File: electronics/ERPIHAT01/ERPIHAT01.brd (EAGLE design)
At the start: 65 x 56 mm, 34 parts, among them J1 CONN-RECT-4PINJST-PH-2MM, J2 CONN-RECT-4PINJST-PH-2MM, J3 CONN-HDMI, J4 CON-FFC-SFW15R, J5 CONN-RECT-3PINJST_PH_2MM, K1 RPI_GPIO, Q1 DMG2305UX, Q2 DMMT5401, Q3 MMBT2222A, U1 EEPROM24, U6 LM2576-D2T

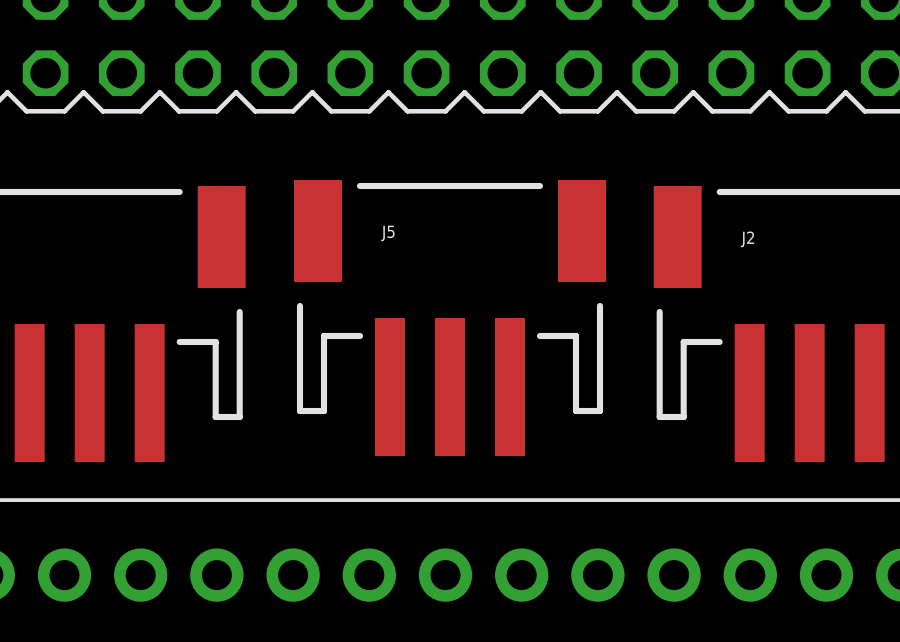
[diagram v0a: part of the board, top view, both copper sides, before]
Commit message: Changed power connector from 3-pin to 2-pin
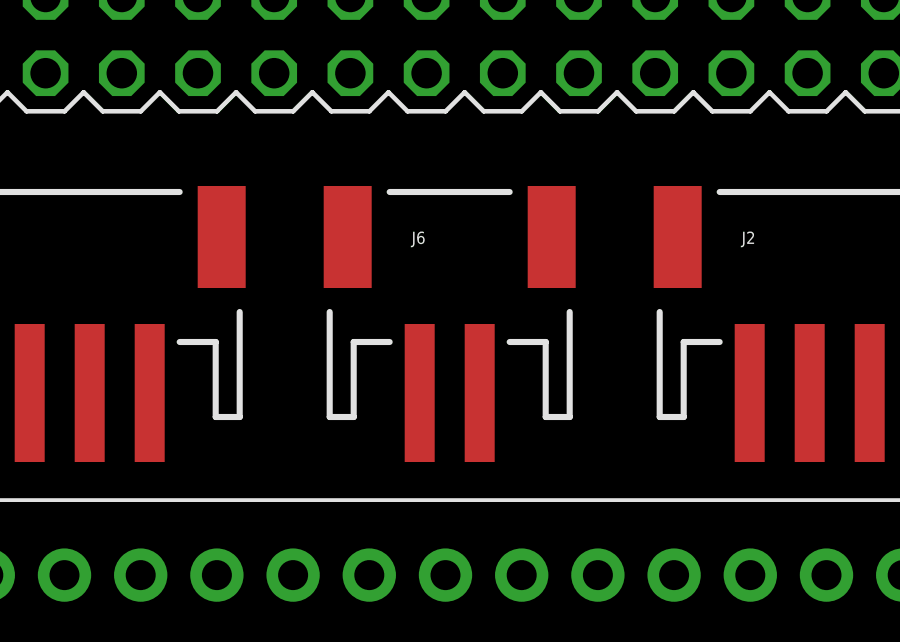
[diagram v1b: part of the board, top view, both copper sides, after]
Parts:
- removed J5: CONN-RECT-3PINJST_PH_2MM, FirePick:CONN-JST_PH-2.0MM-3PIN-SMT-RA
- added J6: CONN-RECT-2PIN, FirePick:CONN-JST_PH-2.0MM-2PIN-SMT-RA
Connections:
- net 12V: now also J6.2; no longer J5.1
- net GND: now also J6.1; no longer J5.3
- net GPIO7: no longer J5.2
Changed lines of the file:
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@@
 <element name="D1" library="diode" package="DO-214AC" value="" x="54" y="29" rot="R180"/>
 <element name="C4" library="rcl" package="PANASONIC_D" value="470uF" x="38" y="27" rot="R90"/>
-<element name="J5" library="FirePick" package="CONN-JST_PH-2.0MM-3PIN-SMT-RA" value="CONN-RECT-3PINJST_PH_2MM" x="32" y="43"/>
+<element name="J6" library="FirePick" package="CONN-JST_PH-2.0MM-2PIN-SMT-RA" value="CONN-RECT-2PIN" x="32" y="43"/>
 </elements>
 <signals>
@@
 <contactref element="D1" pad="A"/>
 <contactref element="C4" pad="-"/>
-<contactref element="J5" pad="3"/>
-<wire x1="78.5025" y1="47.075" x2="80" y2="42.485" width="0" layer="19" extent="1-1"/>
+<contactref element="J6" pad="1"/>
+<wire x1="78.5025" y1="47.075" x2="87" y2="54" width="0" layer="19" extent="1-1"/>
 <wire x1="75.645" y1="46.865" x2="78.5025" y2="47.075" width="0" layer="19" extent="1-1"/>
 <wire x1="74.375" y1="46.865" x2="75.645" y2="46.865" width="0" layer="19" extent="1-1"/>
 <wire x1="73.105" y1="46.865" x2="74.375" y2="46.865" width="0" layer="19" extent="1-1"/>
 <wire x1="71.835" y1="46.865" x2="73.105" y2="46.865" width="0" layer="19" extent="1-1"/>
-<wire x1="56.63" y1="51.23" x2="71.835" y2="46.865" width="0" layer="19" extent="1-1"/>
+<wire x1="73.1" y1="51" x2="73.105" y2="46.865" width="0" layer="19" extent="1-1"/>
+<wire x1="74.1" y1="53" x2="73.1" y2="51" width="0" layer="19" extent="1-1"/>
+<wire x1="70" y1="54" x2="74.1" y2="53" width="0" layer="19" extent="1-1"/>
+<wire x1="80" y1="42.485" x2="78.5025" y2="47.075" width="0" layer="19" extent="1-1"/>
+<wire x1="56.63" y1="51.23" x2="70" y2="54" width="0" layer="19" extent="1-1"/>
 <wire x1="49.01" y1="53.77" x2="56.63" y2="51.23" width="0" layer="19" extent="1-1"/>
 <wire x1="43.93" y1="53.77" x2="49.01" y2="53.77" width="0" layer="19" extent="1-1"/>
 <wire x1="38.85" y1="51.23" x2="43.93" y2="53.77" width="0" layer="19" extent="1-1"/>
-<wire x1="87" y1="54" x2="38.85" y2="51.23" width="0" layer="19" extent="1-1"/>
 <wire x1="31.23" y1="53.77" x2="38.85" y2="51.23" width="0" layer="19" extent="1-1"/>
 <wire x1="23.61" y1="53.77" x2="31.23" y2="53.77" width="0" layer="19" extent="1-1"/>
 <wire x1="18.53" y1="51.23" x2="23.61" y2="53.77" width="0" layer="19" extent="1-1"/>
 <wire x1="13.45" y1="53.77" x2="18.53" y2="51.23" width="0" layer="19" extent="1-1"/>
-<wire x1="70" y1="54" x2="23.61" y2="53.77" width="0" layer="19" extent="1-1"/>
-<wire x1="74.1" y1="53" x2="70" y2="54" width="0" layer="19" extent="1-1"/>
-<wire x1="73.1" y1="51" x2="74.1" y2="53" width="0" layer="19" extent="1-1"/>
-<wire x1="22" y1="40.57" x2="70" y2="54" width="0" layer="19" extent="1-1"/>
+<wire x1="22" y1="40.57" x2="18.53" y2="51.23" width="0" layer="19" extent="1-1"/>
 <wire x1="19.16" y1="34.5" x2="22" y2="40.57" width="0" layer="19" extent="1-1"/>
 <wire x1="18.95" y1="25" x2="19.16" y2="34.5" width="0" layer="19" extent="1-1"/>
-<wire x1="14.81" y1="18.25" x2="18.95" y2="25" width="0" layer="19" extent="1-1"/>
+<wire x1="13.86" y1="22.25" x2="18.95" y2="25" width="0" layer="19" extent="1-1"/>
+<wire x1="14.81" y1="18.25" x2="13.86" y2="22.25" width="0" layer="19" extent="1-1"/>
 <wire x1="14.81" y1="16.75" x2="14.81" y2="18.25" width="0" layer="19" extent="1-1"/>
 <wire x1="14.81" y1="16.25" x2="14.81" y2="16.75" width="0" layer="19" extent="1-1"/>
@@
 <wire x1="14.81" y1="10.75" x2="14.81" y2="11.25" width="0" layer="19" extent="1-1"/>
 <wire x1="13.86" y1="7.75" x2="14.81" y2="10.75" width="0" layer="19" extent="1-1"/>
-<wire x1="13.86" y1="22.25" x2="14.81" y2="18.25" width="0" layer="19" extent="1-1"/>
 <wire x1="8.91" y1="22.85" x2="13.86" y2="22.25" width="0" layer="19" extent="1-1"/>
 <wire x1="8.91" y1="7.15" x2="13.86" y2="7.75" width="0" layer="19" extent="1-1"/>
-<wire x1="9" y1="34.5" x2="8.91" y2="22.85" width="0" layer="19" extent="1-1"/>
 <wire x1="11.825" y1="2" x2="8.91" y2="7.15" width="0" layer="19" extent="1-1"/>
-<wire x1="48" y1="40.57" x2="56.63" y2="51.23" width="0" layer="19" extent="1-1"/>
-<wire x1="56.6" y1="34" x2="48" y2="40.57" width="0" layer="19" extent="1-1"/>
-<wire x1="51.975" y1="29" x2="56.6" y2="34" width="0" layer="19" extent="1-1"/>
+<wire x1="9" y1="34.5" x2="19.16" y2="34.5" width="0" layer="19" extent="1-1"/>
+<wire x1="48" y1="40.57" x2="49.01" y2="53.77" width="0" layer="19" extent="1-1"/>
+<wire x1="47.1" y1="34.5" x2="48" y2="40.57" width="0" layer="19" extent="1-1"/>
+<wire x1="51.975" y1="29" x2="47.1" y2="34.5" width="0" layer="19" extent="1-1"/>
 <wire x1="50.596" y1="23.33" x2="51.975" y2="29" width="0" layer="19" extent="1-1"/>
 <wire x1="54" y1="23.33" x2="50.596" y2="23.33" width="0" layer="19" extent="1-1"/>
-<wire x1="47.1" y1="34.5" x2="51.975" y2="29" width="0" layer="19" extent="1-1"/>
+<wire x1="56.6" y1="34" x2="51.975" y2="29" width="0" layer="19" extent="1-1"/>
 <wire x1="54" y1="13" x2="54" y2="23.33" width="0" layer="19" extent="1-1"/>
 <wire x1="40.5" y1="18" x2="50.596" y2="23.33" width="0" layer="19" extent="1-1"/>
@@
 <wire x1="40.5" y1="9" x2="40.5" y2="12" width="0" layer="19" extent="1-1"/>
 <wire x1="38" y1="24.6" x2="40.5" y2="18" width="0" layer="19" extent="1-1"/>
-<wire x1="30.01" y1="40.77" x2="8.91" y2="7.15" width="0" layer="19" extent="1-1"/>
+<wire x1="33" y1="40.57" x2="8.91" y2="7.15" width="0" layer="19" extent="1-1"/>
 </signal>
 <signal name="+3V3">
@@
 <signal name="GPIO7">
 <contactref element="K1" pad="26"/>
-<contactref element="J5" pad="2"/>
-<wire x1="32.01" y1="40.77" x2="38.85" y2="53.77" width="0" layer="19" extent="1-1"/>
 </signal>
 <signal name="GPIO12">
@@
 <contactref element="C7" pad="+"/>
 <contactref element="U6" pad="1"/>
-<contactref element="J5" pad="1"/>
+<contactref element="J6" pad="2"/>
 <wire x1="57.404" y1="23.33" x2="61.4" y2="34" width="0" layer="19" extent="1-1"/>
-<wire x1="34.01" y1="40.77" x2="57.404" y2="23.33" width="0" layer="19" extent="1-1"/>
+<wire x1="31" y1="40.57" x2="57.404" y2="23.33" width="0" layer="19" extent="1-1"/>
 </signal>
 <signal name="N$7">

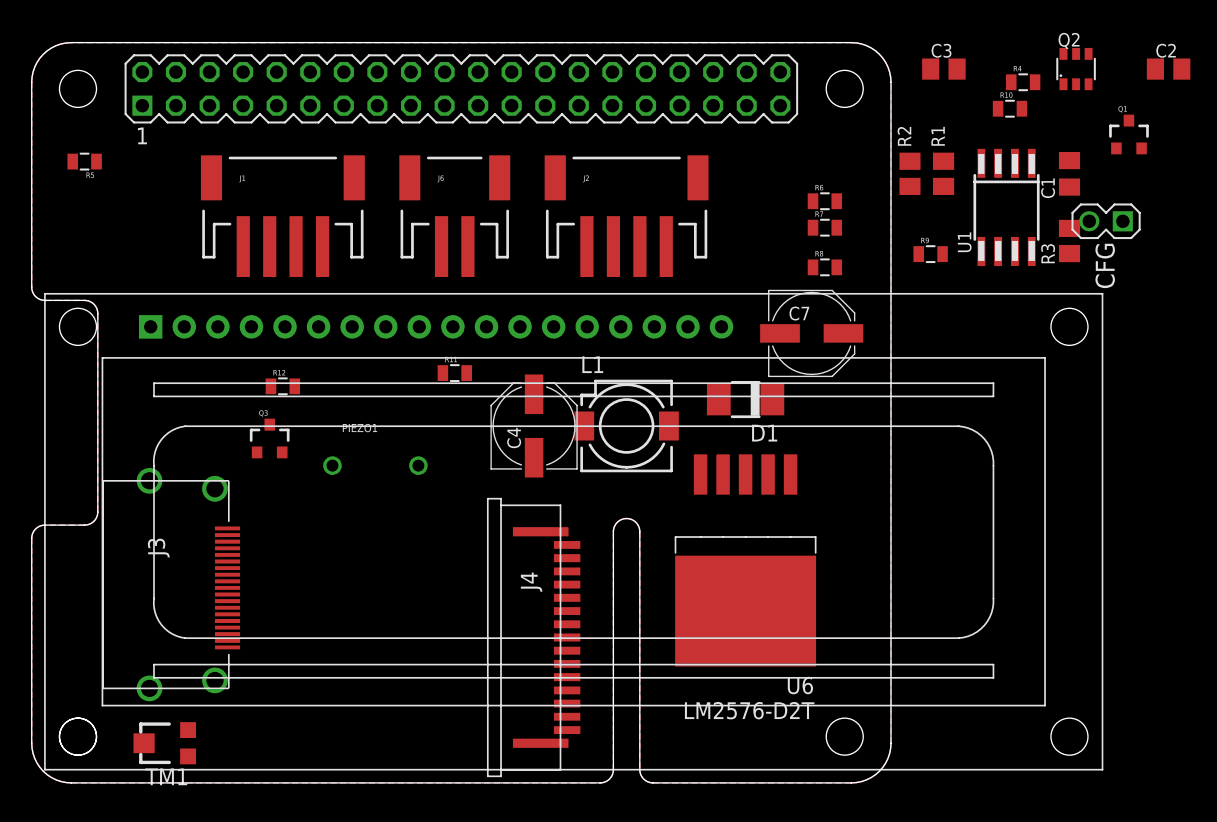
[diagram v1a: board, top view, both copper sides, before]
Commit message: Cleaned up ERPIHAT01 board and finalized for peer review
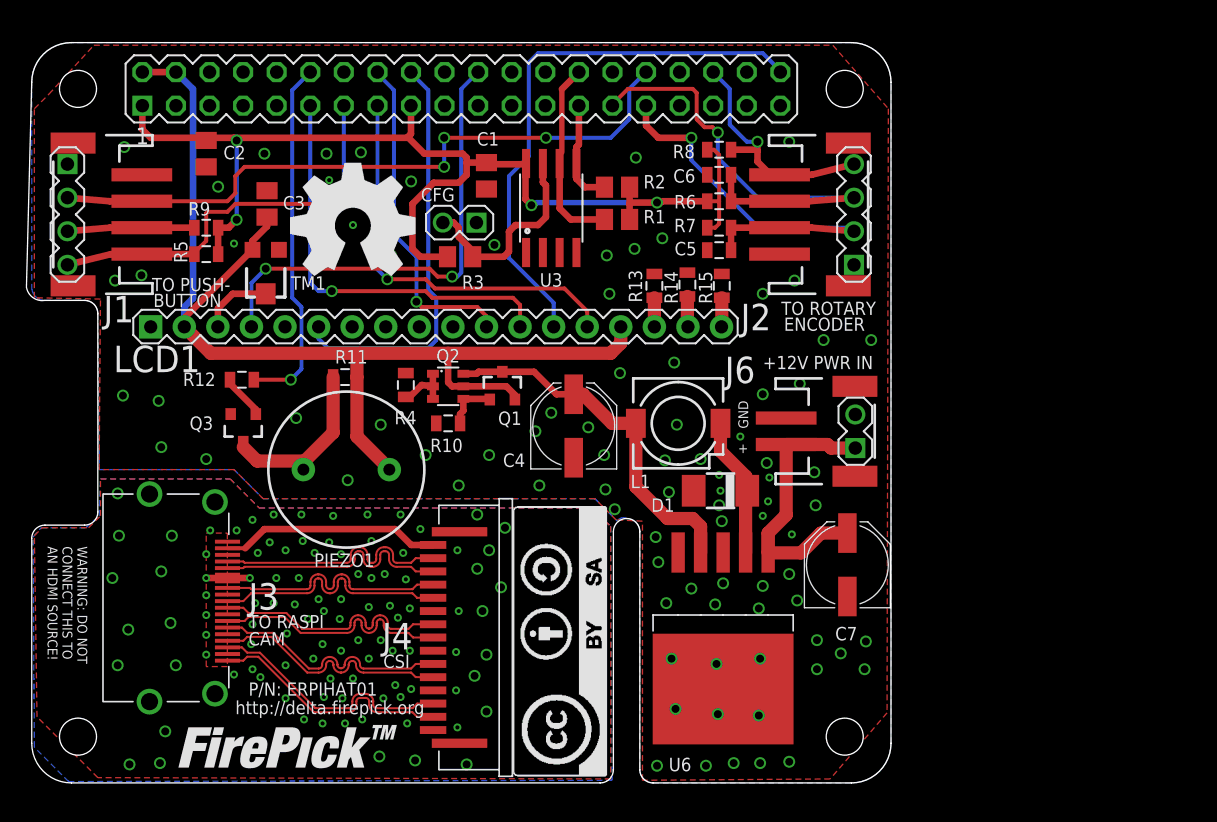
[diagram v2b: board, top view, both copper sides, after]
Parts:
- removed U1: EEPROM24, FLYFISH:SOIC8
- added C5, C6: 100nF, SparkFun-Capacitors:0805
- added J1A, J2A: (no value), !con-lstb:MA04-1
- added J6A: (no value), !con-lstb:MA02-1
- added LOGO1: LOGO-FIREPICK, FirePick:LOGO-FIREPICK
- added LOGO2: LOGO-OSHWMEDIUM, FirePick:LOGO-OSHW-MEDIUM
- added LOGO3: LOGO-CC-BY-SA, FirePick:LOGO-CC-BY-SA
- added R13, R14, R15: ?, SparkFun-Passives:0805
- added U3: (no value), SparkFun-DigitalIC:SO08-EIAJ
- J4: value CON-FFC-SFW15R -> CONN-FFC-SFW15R; device !NJ SMT:CON-FFC-SFW15R -> FirePick:CON-FFC-SFW15R
- PIEZO1: value BUZZERNS -> BUZZERPTH; device !SparkFun-2010-04-13:BUZZER-12MM-NS -> !SparkFun-2010-04-13:BUZZER-12MM
- moved C2 73.1 mm to (13.2, 47.6), turned to 270 degrees
- moved R9 54.8 mm to (13.2, 42.0)
- moved Q2 53.2 mm to (31.5, 30.0), turned to 270 degrees
- moved C3 52.2 mm to (17.8, 43.8), turned to 90 degrees
- moved R4 52.0 mm to (28.3, 30.1), turned to 270 degrees
- moved Q1 51.1 mm to (35.6, 30.0)
- moved CFG 48.9 mm to (32.4, 42.4)
- moved R10 48.7 mm to (31.5, 27.2)
- moved R3 46.1 mm to (32.4, 39.8), turned to 180 degrees
- moved C1 44.1 mm to (34.4, 45.9), turned to 270 degrees
- moved TM1 36.3 mm to (17.7, 38.5), turned to 180 degrees
- moved J6 32.0 mm to (59.5, 26.6), turned to 270 degrees
- moved R1 24.9 mm to (44.3, 42.6), turned to 0 degrees
- moved R2 22.2 mm to (44.3, 45.1), turned to 0 degrees
- moved C7 17.7 mm to (61.7, 16.5), turned to 90 degrees
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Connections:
- net N$2 renamed BUZZ
- net N$7 renamed VOUT
- net N$8 renamed FEEDBACK
- net SCL0 renamed CAM_SCLSDA_N
- net SDA0 renamed CAM_SCLSDA_P
- net VCC renamed N$1
- removed net 3.3V: R5.2, R6.2, R7.2, R8.2
- removed net CAM1_CN: J3.12, J4.8
- removed net CAM1_CP: J3.10, J4.9
- removed net CAM1_DN0: J3.9, J4.2
- removed net CAM1_DN1: J3.6, J4.5
- removed net CAM1_DP0: J3.7, J4.3
- removed net CAM1_DP1: J3.4, J4.6
- removed net CAM_CLK: J3.1, J4.12
- removed net CAM_GPIO: J3.19, J4.11
- removed net N$3: CFG.1, R3.1, U1.7
- removed net PANEL_ENC_A: J2.3, R6.1
- removed net PANEL_ENC_B: J2.2, R7.1
- removed net PANEL_ENC_SW: J2.4, R8.1
- removed net PANEL_LED_GRN: J1.2, R9.1, R9.2
- removed net PANEL_PUSHBTN: J1.4, R5.1
- new net BLUE: LCD1.18, R15.1
- new net CAM_0_N: J3.1, J4.2
- new net CAM_0_P: J3.3, J4.3
- new net CAM_1_N: J3.4, J4.5
- new net CAM_1_P: J3.6, J4.6
- new net CAM_C_N: J3.7, J4.8
- new net CAM_C_P: J3.9, J4.9
- new net CAM_GND: J3.11, J3.13, J3.14, J3.17, J3.2, J3.5, J3.8, J3.SHIELD1, J3.SHIELD2, J3.SHIELD3, J3.SHIELD4, J4.1, J4.10, J4.4, J4.7
- new net CAM_GPIOCLK_N: J3.10, J4.11
- new net CAM_GPIOCLK_P: J3.12, J4.12
- new net GREEN: LCD1.17, R14.1
- new net N$7: CFG.2, R3.1, U3.7
- new net RED: LCD1.16, R13.1
- net +3V3: now also R5.2, R6.2, R7.2, R8.2, R9.2, U3.8; no longer U1.8
- net 12V: now also J6.1, J6A.1; no longer J6.2
- net GND: now also C5.2, C6.2, CFG.1, J1A.1, J2A.1, J6.2, J6A.2, R13.2, R14.2, R15.2, U3.1, U3.2, U3.3, U3.4; no longer CFG.2, J3.11, J3.13, J3.14, J3.17, J3.2, J3.3, J3.5, J3.8, J3.SHIELD1, J3.SHIELD2, J3.SHIELD3, J3.SHIELD4, J4.1, J4.10, J4.4, J4.7, J6.1, LCD1.16, U1.1, U1.2, U1.3, U1.4
- net GPIO12: now also J1.2, J1A.2
- net GPIO16: now also J2.4, J2A.4, R8.1
- net GPIO27: now also J1.4, J1A.4, R5.1
- net GPIO5: now also C6.1, J2.3, J2A.3, R6.1
- net GPIO6: now also C5.1, J2.2, J2A.2, R7.1
- net ID_SC: now also U3.6; no longer U1.6
- net ID_SD: now also U3.5; no longer U1.5
- net PANEL_LED_RED: now also J1A.3, R9.1
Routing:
- net +5V: track 0.00 -> 87.1 mm
- net +3V3: track 0.00 -> 86.5 mm, vias 0 -> 4
- net GPIO12: track 0.00 -> 51.2 mm, vias 0 -> 3
- net GPIO21: track 0.00 -> 42.0 mm
- net GPIO5: track 0.00 -> 35.9 mm, vias 0 -> 1
- net GPIO25: track 0.00 -> 35.7 mm, vias 0 -> 2
- net GPIO6: track 0.00 -> 32.6 mm, vias 0 -> 1
- net GPIO17: track 0.00 -> 31.6 mm, vias 0 -> 1
- net GPIO24: track 0.00 -> 31.4 mm
- net GPIO22: track 0.00 -> 30.7 mm, vias 0 -> 1
- net GPIO27: track 0.00 -> 30.7 mm, vias 0 -> 1
- net FEEDBACK: track 0.00 -> 27.6 mm
- net GPIO18: track 0.00 -> 27.3 mm, vias 0 -> 1
- net GPIO23: track 0.00 -> 25.1 mm, vias 0 -> 1
- net 12V: track 0.00 -> 20.7 mm
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- added copper zone on layer 1, net CAM_GND
- added copper zone on layer 16, net CAM_GND
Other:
- board size 65 x 56 mm -> 65.4 x 56 mm
- board text added: "!E"
- board text added: "!RW"
- board text added: "+"
- board text added: "+12V PWR IN"
- board text added: "+12VDC IN"
- board text added: "BACKLIGHT ANODE"
- board text added: "BACKLIGHT CATHODE (BLUE)"
- board text added: "BACKLIGHT CATHODE (GREEN)"
- board text added: "BACKLIGHT CATHODE (RED)"
- board text added: "BUTTON"
- board text added: "CAM"
- board text added: "COM"
- board text added: "CONTRAST"
- board text added: "CSI"
- board text added: "DB0"
- board text added: "DB1"
- board text added: "DB2"
- board text added: "DB3"
- board text added: "DB4"
- board text added: "DB5"
- board text added: "DB6"
- board text added: "DB7"
- board text added: "ENC A"
- board text added: "ENC B"
- board text added: "ENC SW"
- board text added: "ENCODER"
- board text added: "GND"
- board text added: "LED A"
- board text added: "LED K"
- board text added: "P/N: ERPIHAT01"
- board text added: "RS"
- board text added: "SW1"
- board text added: "SW2"
- board text added: "TO PUSH-"
- board text added: "TO RASPI"
- board text added: "TO ROTARY"
- board text added: "VDD"
- board text added: "WARNING: DO NOT CONNECT THIS TO AN HDMI SOURCE!"
- board text added: "http://delta.firepick.org"

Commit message: Revision A, after assembling first batch of PCBs.
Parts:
- C1, C2, C3, C5, C6: value 100nF -> 0.1uF
- C4: value 470uF -> 470 uF 25V
- R1, R2: value 3k9 -> 4.7K
- R12: value 1k? -> 1K
- R13: value ? -> 0
- R14: value ? -> 5.6k
- R15: value ? -> DNP
- moved LOGO3 30.5 mm to (14.2, 9.00), turned to 0 degrees
- moved J3 5.95 mm to (5.60, 16.5)
- moved J4 4.90 mm to (38.3, 11.0), turned to 270 degrees
- moved LOGO1 3.11 mm to (11.1, 2.50)
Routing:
- net N$1: track 16.6 -> 47.4 mm, vias 0 -> 2
- net CAM_SCLSDA_P: track 18.5 -> 46.0 mm, vias 0 -> 2
- net CAM_SCLSDA_N: track 18.5 -> 44.6 mm, vias 0 -> 2
- net CAM_GPIOCLK_P: track 18.2 -> 44.4 mm, vias 0 -> 2
- net CAM_C_P: track 18.5 -> 44.4 mm, vias 0 -> 2
- net CAM_GPIOCLK_N: track 18.5 -> 44.4 mm, vias 0 -> 2
- net CAM_C_N: track 18.5 -> 44.4 mm, vias 0 -> 2
- net CAM_1_P: track 18.5 -> 44.1 mm, vias 0 -> 2
- net CAM_1_N: track 18.5 -> 44.1 mm
- net CAM_0_N: track 18.7 -> 44.1 mm, vias 0 -> 2
- net CAM_0_P: track 18.8 -> 44.1 mm, vias 0 -> 2
- net CAM_GND: track 4.61 -> 11.2 mm, vias 101 -> 55
- net GPIO27: track 30.7 -> 32.3 mm
- net GPIO16: track 18.5 -> 20.0 mm
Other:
- board size 65.4 x 56 mm -> 65 x 56 mm
